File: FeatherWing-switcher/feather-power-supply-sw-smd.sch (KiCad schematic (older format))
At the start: 29 parts, among them J1 5.08mm, J2 Conn_01x12, J3 Conn_01x16, J4 QWIIC, J5 0.1\"x4, Q1 Q_PMOS_GSD, U1 TPS5405DR

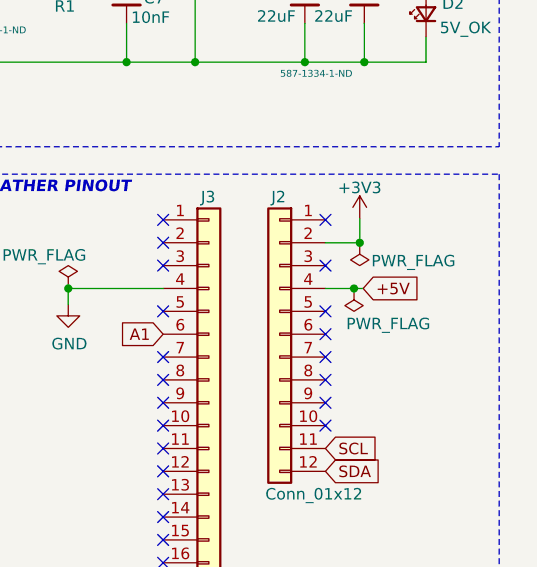
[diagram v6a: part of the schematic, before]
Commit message: fixes 5V bodge and connects vdivider
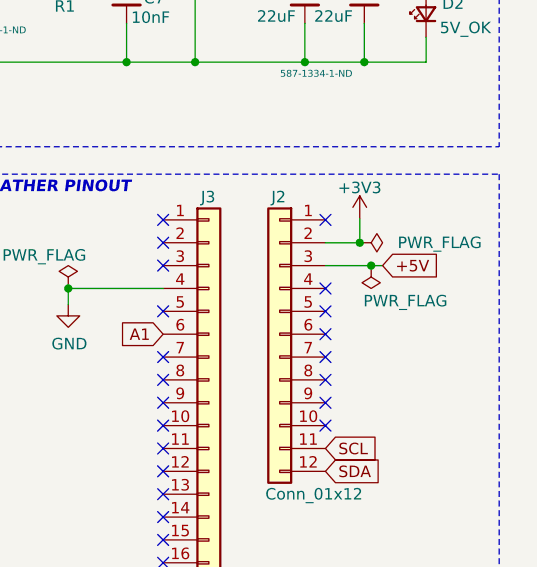
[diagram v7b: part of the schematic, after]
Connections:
- net +5V: now also J2.3 (Pin_3); no longer J2.4 (Pin_4)
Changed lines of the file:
@@
 	1    0    0    -1
 $EndComp
-Text GLabel 7615 3900 2    50   Input ~ 0
+Text GLabel 7700 3800 2    50   Input ~ 0
 +5V
-Wire Wire Line
-	7450 3900 7575 3900
 $Comp
 L power:GND #PWR04
@@
 L power:PWR_FLAG #FLG04
 U 1 1 5F43E163
-P 7575 3900
-F 0 "#FLG04" H 7575 3975 50  0001 C CNN
-F 1 "PWR_FLAG" H 7425 4055 50  0000 C CNN
-F 2 "" H 7575 3900 50  0001 C CNN
-F 3 "~" H 7575 3900 50  0001 C CNN
-	1    7575 3900
+P 7650 3800
+F 0 "#FLG04" H 7650 3875 50  0001 C CNN
+F 1 "PWR_FLAG" H 7500 3955 50  0000 C CNN
+F 2 "" H 7650 3800 50  0001 C CNN
+F 3 "~" H 7650 3800 50  0001 C CNN
+	1    7650 3800
 	-1   0    0    1
 $EndComp
-Connection ~ 7575 3900
-Wire Wire Line
-	7575 3900 7615 3900
 $Comp
 L power:PWR_FLAG #FLG03
@@
 $EndComp
 Connection ~ 6325 3900
-NoConn ~ 7450 3800
 NoConn ~ 7450 4000
 NoConn ~ 7450 4100
@@
 P 7600 3700
 F 0 "#FLG02" H 7600 3775 50  0001 C CNN
-F 1 "PWR_FLAG" H 7365 3780 50  0000 C CNN
+F 1 "PWR_FLAG" V 7600 4050 50  0000 C CNN
 F 2 "" H 7600 3700 50  0001 C CNN
 F 3 "~" H 7600 3700 50  0001 C CNN
 	1    7600 3700
-	-1   0    0    1
+	0    1    1    0
 $EndComp
 Connection ~ 7600 3700
@@
 Wire Wire Line
 	7620 2170 7890 2170
+Wire Wire Line
+	7450 3800 7650 3800
+Connection ~ 7650 3800
+Wire Wire Line
+	7650 3800 7700 3800
+NoConn ~ 7450 3900
 $EndSCHEMATC

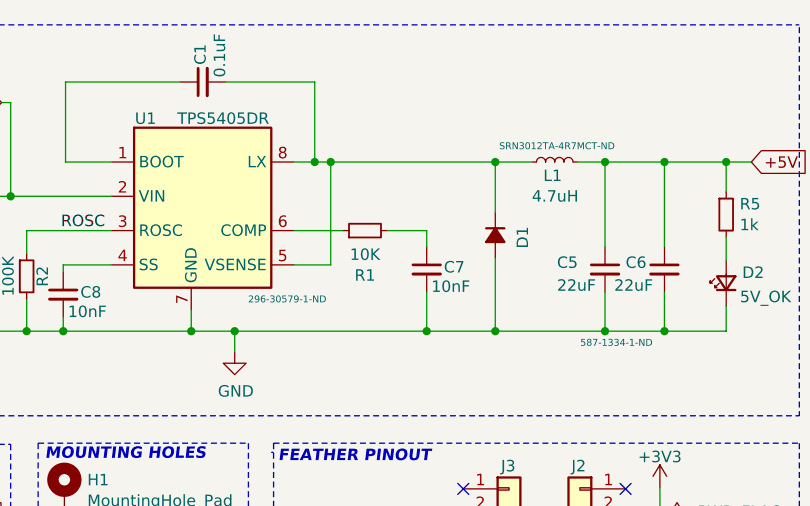
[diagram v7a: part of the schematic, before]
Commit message: v2.1 fix vsense wiring and update layout
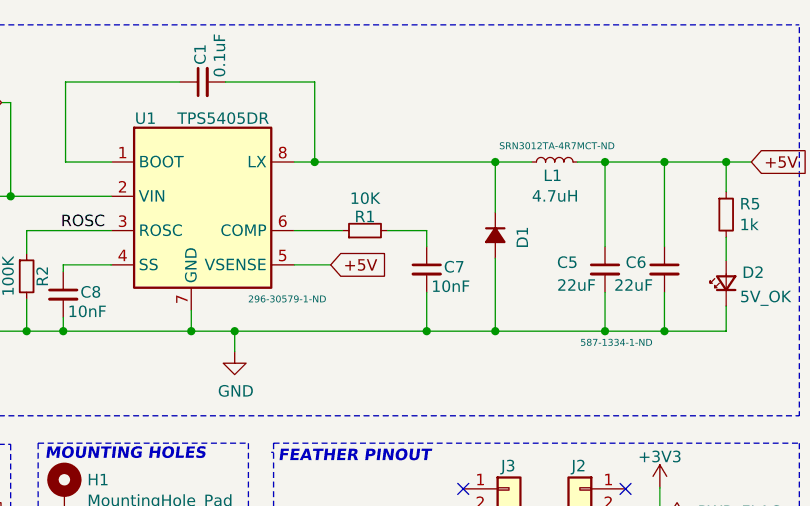
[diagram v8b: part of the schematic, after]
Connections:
- net +5V: now also U1.5 (VSENSE)
- net at C1.2, D1.1 (K), L1.1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: no longer U1.5 (VSENSE)
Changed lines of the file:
@@
 Sheet 1 1
 Title "Feather Switcher"
-Date "2020-10-05"
-Rev "2.0"
+Date "2020-10-25"
+Rev "2.1"
 Comp ""
 Comment1 "Adafruit FeatherWing compatible 5V switching power supply"
@@
 U 1 1 5F4EB99E
 P 6310 2470
-F 0 "R1" V 6114 2470 50  0000 C CNN
-F 1 "10K" V 6205 2470 50  0000 C CNN
+F 0 "R1" V 6370 2470 50  0000 C CNN
+F 1 "10K" V 6450 2470 50  0000 C CNN
 F 2 "Resistor_SMD:R_0603_1608Metric_Pad1.05x0.95mm_HandSolder" H 6310 2470 50  0001 C CNN
 F 3 "~" H 6310 2470 50  0001 C CNN
@@
 	6090 2170 6000 2170
 Wire Wire Line
-	6090 2170 6160 2170
-Wire Wire Line
 	6880 2170 6880 2390
 Connection ~ 6090 2170
@@
 Wire Wire Line
 	6000 2620 6160 2620
-Wire Wire Line
-	6160 2620 6160 2170
 Connection ~ 4330 2910
 Wire Wire Line
@@
 Wire Notes Line
 	5910 3400 5910 5300
-Wire Wire Line
-	6880 2170 6160 2170
 Connection ~ 6880 2170
-Connection ~ 6160 2170
 Wire Wire Line
 	6880 2910 6580 2910
@@
 	7650 3800 7700 3800
 NoConn ~ 7450 3900
+Wire Wire Line
+	6090 2170 6880 2170
+Text GLabel 6160 2620 2    50   Input ~ 0
++5V
 $EndSCHEMATC
